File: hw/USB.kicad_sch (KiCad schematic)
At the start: 3 parts, among them J2 USB

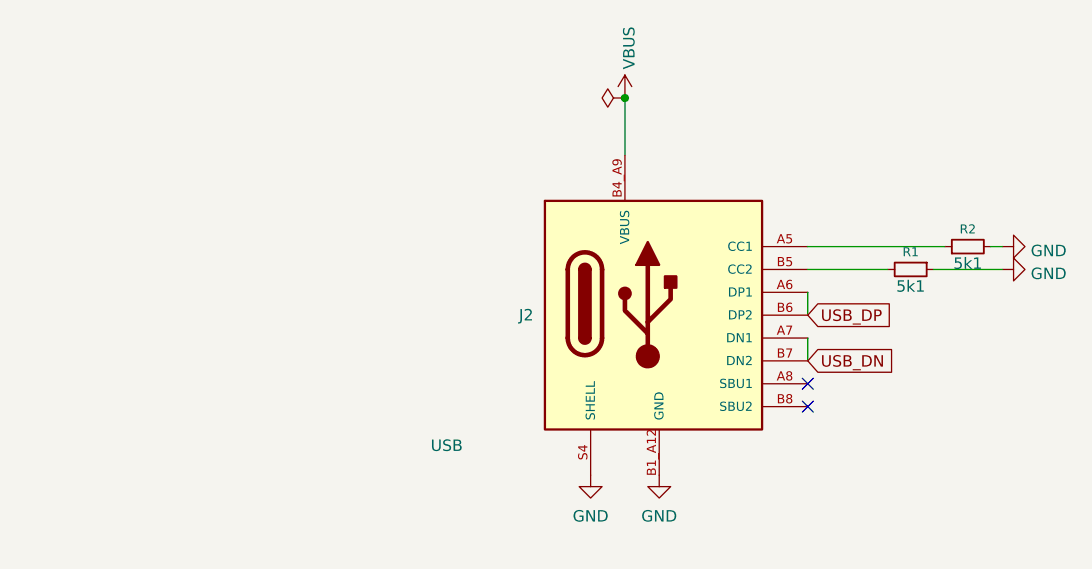
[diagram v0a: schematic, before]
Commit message: hw: use parts from LCSC
Signed-off-by: Mahyar Koshkouei <mk@deltabeard.com>
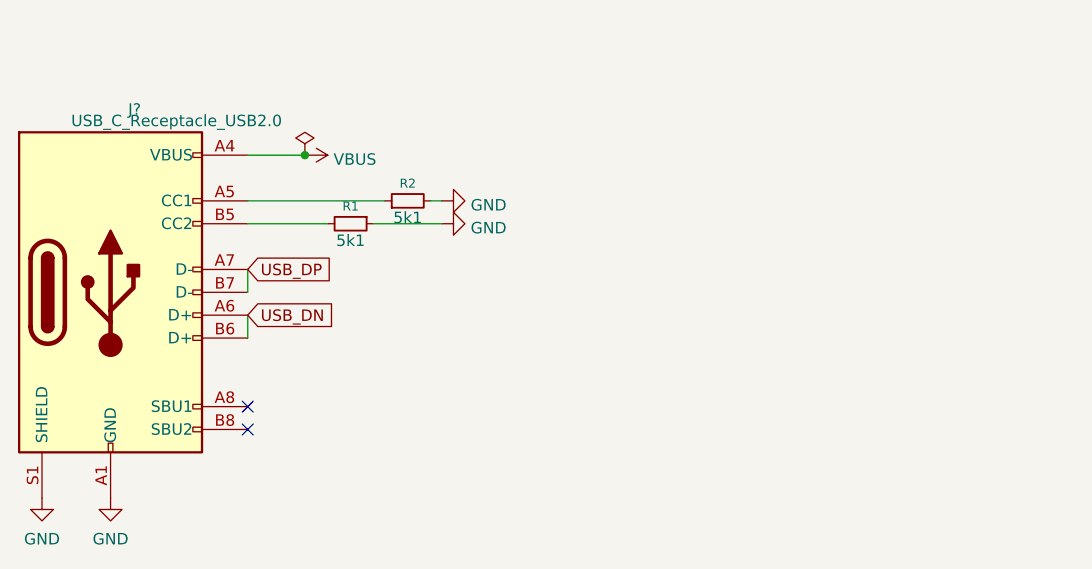
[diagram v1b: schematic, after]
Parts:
- removed J2: USB, Project_Specific:GCT_USB4105-GF-A, symbol Project_specific:USB4105-GF-A
- added J?: USB_C_Receptacle_USB2.0, symbol Connector:USB_C_Receptacle_USB2.0
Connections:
- net GND: now also J?.A1 (GND), J?.A12 (GND), J?.B1 (GND), J?.B12 (GND), J?.S1 (SHIELD)
- net USB_DN: now also J?.A6 (D+), J?.B6 (D+)
- net USB_DP: now also J?.A7 (D-), J?.B7 (D-)
- net VBUS: now also J?.A4 (VBUS), J?.A9 (VBUS), J?.B4 (VBUS), J?.B9 (VBUS)
- net at R2.1: now also J?.A5 (CC1)
- net at R1.2: now also J?.B5 (CC2)
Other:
- moved on the sheet: R1, R2

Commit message: hw: complete 2-layer PCB
Signed-off-by: Mahyar Koshkouei <mk@deltabeard.com>
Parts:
- J2: renamed from J?; footprint (none) -> Connector_USB:USB_C_Receptacle_Palconn_UTC16-G; LCSC (none) -> C167321; MFr (none) -> 918-418K2023S40001
- R1, R2: LCSC (none) -> C23186
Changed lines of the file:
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@@
   (symbol (lib_id "power:VBUS") (at 95.25 72.39 270) (unit 1)
     (in_bom yes) (on_board yes) (fields_autoplaced)
-    (property "Reference" "#PWR028" (id 0) (at 91.44 72.39 0)
+    (property "Reference" "#PWR024" (id 0) (at 91.44 72.39 0)
       (effects (font (size 1.27 1.27)) hide)
     )
@@
   (symbol (lib_id "power:GND") (at 66.04 110.49 0) (unit 1)
     (in_bom yes) (on_board yes) (fields_autoplaced)
-    (property "Reference" "#PWR027" (id 0) (at 66.04 116.84 0)
+    (property "Reference" "#PWR022" (id 0) (at 66.04 116.84 0)
       (effects (font (size 1.27 1.27)) hide)
     )
@@
   (symbol (lib_id "power:GND") (at 73.66 110.49 0) (unit 1)
     (in_bom yes) (on_board yes) (fields_autoplaced)
-    (property "Reference" "#PWR029" (id 0) (at 73.66 116.84 0)
+    (property "Reference" "#PWR023" (id 0) (at 73.66 116.84 0)
       (effects (font (size 1.27 1.27)) hide)
     )
@@
   (symbol (lib_id "power:GND") (at 110.49 77.47 90) (unit 1)
     (in_bom yes) (on_board yes) (fields_autoplaced)
-    (property "Reference" "#PWR030" (id 0) (at 116.84 77.47 0)
+    (property "Reference" "#PWR025" (id 0) (at 116.84 77.47 0)
       (effects (font (size 1.27 1.27)) hide)
     )
@@
   (symbol (lib_id "power:GND") (at 110.49 80.01 90) (unit 1)
     (in_bom yes) (on_board yes) (fields_autoplaced)
-    (property "Reference" "#PWR031" (id 0) (at 116.84 80.01 0)
+    (property "Reference" "#PWR026" (id 0) (at 116.84 80.01 0)
       (effects (font (size 1.27 1.27)) hide)
     )
@@
       (effects (font (size 1.27 1.27)) hide)
     )
+    (property "LCSC" "C23186" (id 4) (at 100.33 80.01 0)
+      (effects (font (size 1.27 1.27)) hide)
+    )
     (pin "1")
     (pin "2")
@@
       (effects (font (size 1.27 1.27)) hide)
     )
+    (property "LCSC" "C23186" (id 4) (at 106.68 77.47 0)
+      (effects (font (size 1.27 1.27)) hide)
+    )
     (pin "1")
     (pin "2")
@@
   (symbol (lib_id "Connector:USB_C_Receptacle_USB2.0") (at 73.66 87.63 0) (unit 1)
     (in_bom yes) (on_board yes) (fields_autoplaced)
-    (property "Reference" "J?" (id 0) (at 76.327 67.31 0))
+    (property "Reference" "J2" (id 0) (at 76.327 67.31 0))
     (property "Value" "USB_C_Receptacle_USB2.0" (id 1) (at 92.71 68.58 0)
       (effects (font (size 1.27 1.27)) (justify right))
     )
-    (property "Footprint" "" (id 2) (at 77.47 87.63 0)
+    (property "Footprint" "Connector_USB:USB_C_Receptacle_Palconn_UTC16-G" (id 2) (at 77.47 87.63 0)
       (effects (font (size 1.27 1.27)) hide)
     )
@@
       (effects (font (size 1.27 1.27)) hide)
     )
+    (property "LCSC" "C167321" (id 4) (at 73.66 87.63 0)
+      (effects (font (size 1.27 1.27)) hide)
+    )
+    (property "MFr" "918-418K2023S40001" (id 5) (at 73.66 87.63 0)
+      (effects (font (size 1.27 1.27)) hide)
+    )

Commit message: hw: add more information to BOM
Signed-off-by: Mahyar Koshkouei <mk@deltabeard.com>
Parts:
- J2: Manufacturer (none) -> Jing Extension of the Electronic Co.
- R1, R2: MFr (none) -> 0603WAF5101T5E; Manufacturer (none) -> UNI-ROYAL(Uniroyal Elec); Notes (none) -> Alternative manufacturer is acceptable
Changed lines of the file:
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@@
+      (effects (font (size 1.27 1.27)) hide)
+    )
+    (property "Description" "±1% ±100ppm/℃ 5.1kΩ 0.1W 0603 Chip Resistor - Surface Mount ROHS " (id 5) (at 100.33 80.01 0)
+      (effects (font (size 1.27 1.27)) hide)
+    )
+    (property "MFr" "0603WAF5101T5E" (id 6) (at 100.33 80.01 0)
+      (effects (font (size 1.27 1.27)) hide)
+    )
+    (property "Manufacturer" " UNI-ROYAL(Uniroyal Elec) " (id 7) (at 100.33 80.01 0)
+      (effects (font (size 1.27 1.27)) hide)
+    )
+    (property "Notes" "Alternative manufacturer is acceptable" (id 8) (at 100.33 80.01 0)
       (effects (font (size 1.27 1.27)) hide)
     )
@@
     )
     (property "LCSC" "C23186" (id 4) (at 106.68 77.47 0)
+      (effects (font (size 1.27 1.27)) hide)
+    )
+    (property "Description" "±1% ±100ppm/℃ 5.1kΩ 0.1W 0603 Chip Resistor - Surface Mount ROHS " (id 5) (at 106.68 77.47 0)
+      (effects (font (size 1.27 1.27)) hide)
+    )
+    (property "MFr" "0603WAF5101T5E" (id 6) (at 106.68 77.47 0)
+      (effects (font (size 1.27 1.27)) hide)
+    )
+    (property "Manufacturer" " UNI-ROYAL(Uniroyal Elec) " (id 7) (at 106.68 77.47 0)
+      (effects (font (size 1.27 1.27)) hide)
+    )
+    (property "Notes" "Alternative manufacturer is acceptable" (id 8) (at 106.68 77.47 0)
       (effects (font (size 1.27 1.27)) hide)
     )
@@
       (effects (font (size 1.27 1.27)) hide)
     )
+    (property "Description" " Receptacle USB - Type C 16 SMD USB Connectors ROHS " (id 6) (at 73.66 87.63 0)
+      (effects (font (size 1.27 1.27)) hide)
+    )
+    (property "Manufacturer" " Jing Extension of the Electronic Co. " (id 7) (at 73.66 87.63 0)
+      (effects (font (size 1.27 1.27)) hide)
+    )

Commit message: hw: fix USB
Additionally reduced the size of the battery holder.

Signed-off-by: Mahyar Koshkouei <mk@deltabeard.com>
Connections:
- net USB_DN: now also J2.A7 (D-), J2.B7 (D-); no longer J2.A6 (D+), J2.B6 (D+)
- net USB_DP: now also J2.A6 (D+), J2.B6 (D+); no longer J2.A7 (D-), J2.B7 (D-)
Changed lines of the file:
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@@
     (stroke (width 0) (type solid) (color 0 0 0 0))
   )
-  (global_label "USB_DP" (shape input) (at 88.9 85.09 0) (fields_autoplaced)
+  (global_label "USB_DN" (shape input) (at 88.9 85.09 0) (fields_autoplaced)
     (effects (font (size 1.27 1.27)) (justify left))
-    (property "Intersheet References" "${INTERSHEET_REFS}" (id 0) (at 98.5354 85.0106 0)
+    (property "Intersheet References" "${INTERSHEET_REFS}" (id 0) (at 98.5959 85.0106 0)
       (effects (font (size 1.27 1.27)) (justify left) hide)
     )
   )
-  (global_label "USB_DN" (shape input) (at 88.9 90.17 0) (fields_autoplaced)
+  (global_label "USB_DP" (shape input) (at 88.9 90.17 0) (fields_autoplaced)
     (effects (font (size 1.27 1.27)) (justify left))
-    (property "Intersheet References" "${INTERSHEET_REFS}" (id 0) (at 98.5959 90.0906 0)
+    (property "Intersheet References" "${INTERSHEET_REFS}" (id 0) (at 98.5354 90.0906 0)
       (effects (font (size 1.27 1.27)) (justify left) hide)
     )

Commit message: all: Add open source license
Signed-off-by: Mahyar Koshkouei <mk@deltabeard.com>
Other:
- company: Mahyar Koshkouei -> Copyright (c) 2021 Mahyar Koshkouei
- title: RP2040 Game Boy Cart -> DBGC: RP2040 Game Boy Cart
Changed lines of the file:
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@@
   (paper "A4")
   (title_block
-    (title "RP2040 Game Boy Cart")
+    (title "DBGC: RP2040 Game Boy Cart")
     (date "2021-09-29")
     (rev "0.3a")
-    (company "Mahyar Koshkouei")
-    (comment 1 "All Rights Reserved")
+    (company "Copyright (c) 2021 Mahyar Koshkouei")
+    (comment 1 "CC BY-SA 4.0")
     (comment 2 "Compatible with DMG, MGB, & CGB. Collectively referred to as \"GB\" here.")
   )
